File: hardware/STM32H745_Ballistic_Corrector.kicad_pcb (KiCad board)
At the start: 4 copper layers, 80 x 60 mm, 4 parts

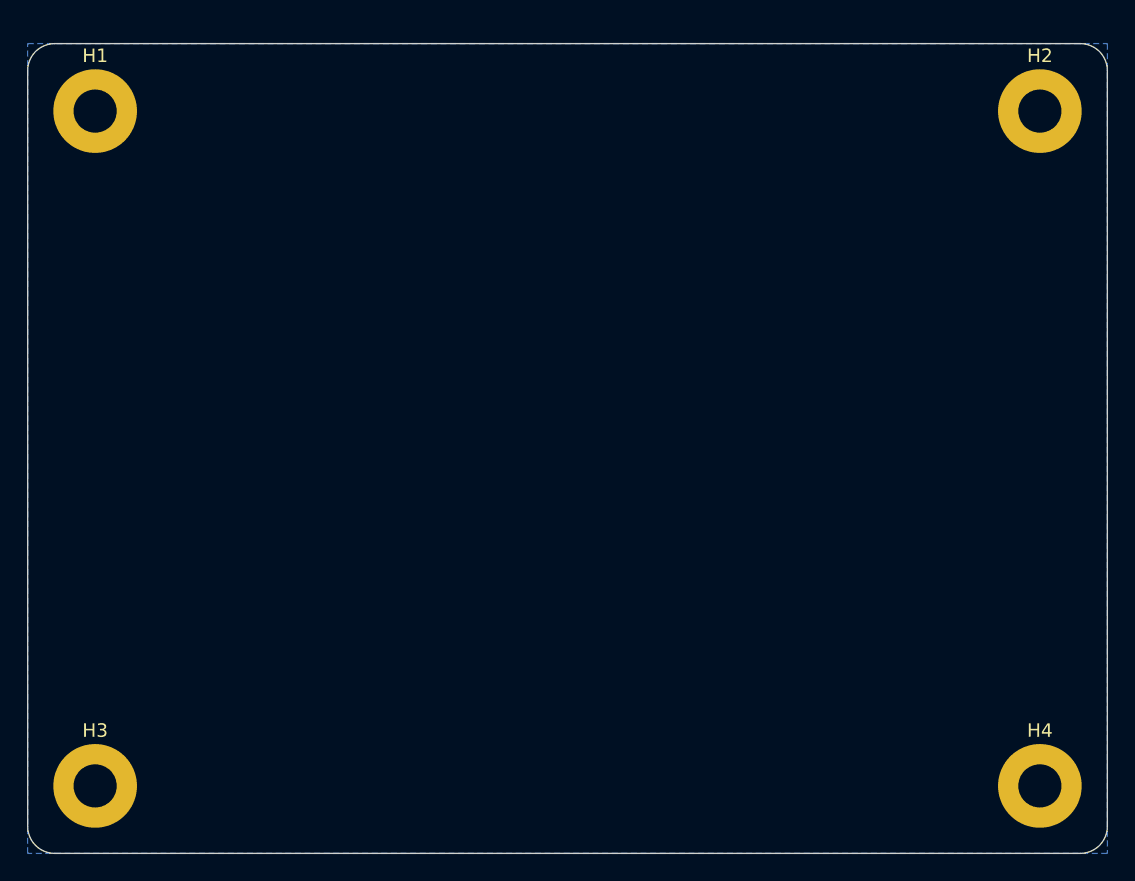
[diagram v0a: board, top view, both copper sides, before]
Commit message: PCB placement pass: 48 component footprints placed per HLD floorplan
Placement generator (tools/gen_pcb_placement.py):
- Reproducible: emits footprints into a marked block of the .kicad_pcb;
  re-running regenerates the block idempotently (deterministic UUIDs)
- Package generators: LQFP-144, QFN-24/28 (+EP), SOIC-8 (150/208 mil),
  MSOP-8, SOT-23-5, SOT-223, LGA-12 (VL53L0X), LGA-10 (BMP390),
  3225 crystal, chip 0402/0805, SMA diode, 4x4 inductor, pin headers
  (1x3, 2x5 1.27mm SWD, 2x7 2.54mm sensor), USB Mini-B, barrel jack,
  slide switch, test points

Placement per HLD_BOARD_INTEGRATION.md §5.3 floorplan:
- POWER row (top edge): J1 12V in -> D1 Schottky -> U2 buck + L1 ->
  U3 3V3 LDO -> U12 1V8 LDO, bulk caps, 6 rail test points TP1-TP6
- DEBUG zone (left): J5 USB, U8 CP2102N, J2 UART header, J3 SWD 2x5,
  SW1 BOOT0, NRST RC (R1/C1), BOOT0 pull-down R4
- MCU zone (center): U1 LQFP-144 at (90,78), Y1 8MHz + 12pF load caps
  in crystal corner, 8x 100nF decoupling ring + 10uF bulk, I2C pull-ups
- MEMORY zone (right): U6 W25Q128JV 25mm from MCU QSPI bank, U7 EEPROM
- SENSOR row (bottom): U5 VL53L0X at board edge (clear aperture),
  U4 ICM-20689 at mount-hole center of mass, U10 MCP9808, U11 BMP390,
  J4 14-pin sensor connector with HLD §5.4 fixed pinout nets

Net binding: power rails, QSPI (U6 full pinout), I2C, SPI, UART, USB
pads pre-assigned to existing PCB nets for ratsnest-guided routing;
provisional until schematic netlist import

Verification: automated courtyard collision + board containment check -
2 initial overlaps (J4/H4, J2/J5) fixed by position adjustment, final
result 52 footprints, 0 overlaps, s-expression balance clean

Co-Authored-By: Claude Fable 5 <noreply@anthropic.com>
Claude-Session: https://claude.ai/code/session_01WTnjtLhvvQkSSzjNBr8Vvw
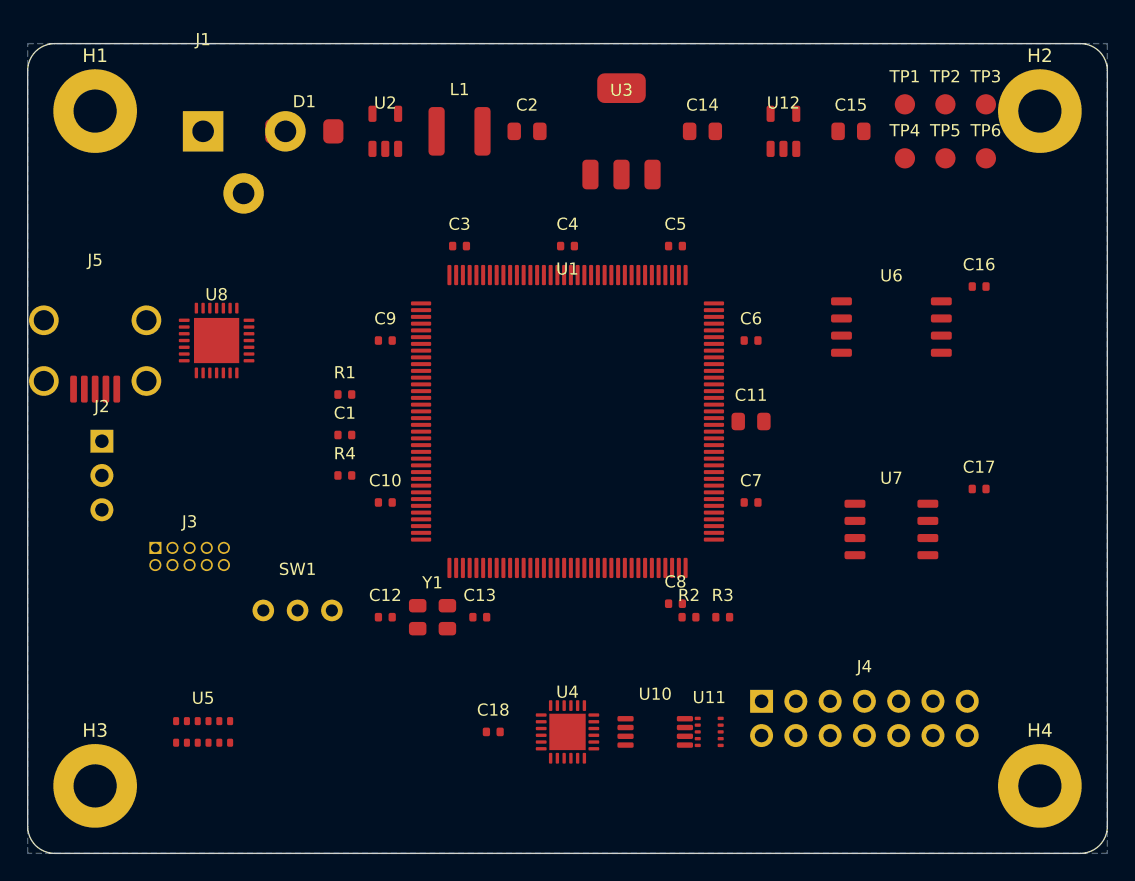
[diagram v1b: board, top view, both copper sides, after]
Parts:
- added C1: 100nF, Capacitor_SMD:C_0402, F.Cu at (73.5, 79.0)
- added C10: 100nF, Capacitor_SMD:C_0402, F.Cu at (76.5, 84.0)
- added C11: 10uF, Capacitor_SMD:C_0805, F.Cu at (103.6, 78.0)
- added C12: 12pF 1%, Capacitor_SMD:C_0402, F.Cu at (76.5, 92.5)
- added C13: 12pF 1%, Capacitor_SMD:C_0402, F.Cu at (83.5, 92.5)
- added C14: 10uF, Capacitor_SMD:C_0805, F.Cu at (100.0, 56.5)
- added C15: 10uF, Capacitor_SMD:C_0805, F.Cu at (111.0, 56.5)
- added C16: 100nF, Capacitor_SMD:C_0402, F.Cu at (120.5, 68.0)
- added C17: 100nF, Capacitor_SMD:C_0402, F.Cu at (120.5, 83.0)
- added C18: 100nF, Capacitor_SMD:C_0402, F.Cu at (84.5, 101.0)
- added C2: 10uF, Capacitor_SMD:C_0805, F.Cu at (87.0, 56.5)
- added C3: 100nF, Capacitor_SMD:C_0402, F.Cu at (82.0, 65.0)
- added C4: 100nF, Capacitor_SMD:C_0402, F.Cu at (90.0, 65.0)
- added C5: 100nF, Capacitor_SMD:C_0402, F.Cu at (98.0, 65.0)
- added C6: 100nF, Capacitor_SMD:C_0402, F.Cu at (103.6, 72.0)
- added C7: 100nF, Capacitor_SMD:C_0402, F.Cu at (103.6, 84.0)
- added C8: 100nF, Capacitor_SMD:C_0402, F.Cu at (98.0, 91.5)
- added C9: 100nF, Capacitor_SMD:C_0402, F.Cu at (76.5, 72.0)
- added D1: 1N5819 SMA, Diode_SMD:D_SMA, F.Cu at (70.5, 56.5)
- added J1: 12V_IN, Connector_BarrelJack:BarrelJack_5.5x2.1mm, F.Cu at (63.0, 56.5)
- added J2: UART_DBG, Connector_PinHeader_2.54mm:PinHeader_1x03, F.Cu at (55.5, 82.0)
- added J3: SWD, Connector_PinHeader_1.27mm:PinHeader_2x05, F.Cu at (62.0, 88.0)
- added J4: SENSOR_14P, Connector_PinHeader_2.54mm:PinHeader_2x07, F.Cu at (112.0, 100.0)
- added J5: USB_MINI_B, Connector_USB:USB_Mini-B, F.Cu at (55.0, 72.0)
- added L1: 4.7uH, Inductor_SMD:L_4x4mm, F.Cu at (82.0, 56.5)
- added R1: 10k, Resistor_SMD:R_0402, F.Cu at (73.5, 76.0)
- added R2: 10k, Resistor_SMD:R_0402, F.Cu at (99.0, 92.5)
- added R3: 10k, Resistor_SMD:R_0402, F.Cu at (101.5, 92.5)
- added R4: 10k, Resistor_SMD:R_0402, F.Cu at (73.5, 82.0)
- added SW1: BOOT0, Button_Switch_THT:SW_Slide, F.Cu at (70.0, 92.0)
- added TP1: VCC_12V, TestPoint:TestPoint_Pad_1.5mm, F.Cu at (115.0, 54.5)
- added TP2: VCC_5V, TestPoint:TestPoint_Pad_1.5mm, F.Cu at (118.0, 54.5)
- added TP3: VCC_3V3, TestPoint:TestPoint_Pad_1.5mm, F.Cu at (121.0, 54.5)
- added TP4: VCC_1V8, TestPoint:TestPoint_Pad_1.5mm, F.Cu at (115.0, 58.5)
- added TP5: GND, TestPoint:TestPoint_Pad_1.5mm, F.Cu at (118.0, 58.5)
- added TP6: GND, TestPoint:TestPoint_Pad_1.5mm, F.Cu at (121.0, 58.5)
- added U1: STM32H745ZIT6, Package_QFP:LQFP-144_20x20mm_P0.5mm, F.Cu at (90.0, 78.0)
- added U10: MCP9808, Package_SO:MSOP-8_3x3mm_P0.65mm, F.Cu at (96.5, 101.0)
- added U11: BMP390, Sensor_Pressure:Bosch_LGA-10, F.Cu at (100.5, 101.0)
- added U12: LDO_1V8_200mA, Package_TO_SOT_SMD:SOT-23-5, F.Cu at (106.0, 56.5)
- added U2: TPS62133A, Package_TO_SOT_SMD:SOT-23-5, F.Cu at (76.5, 56.5)
- added U3: LDO_3V3_500mA, Package_TO_SOT_SMD:SOT-223, F.Cu at (94.0, 56.5)
- added U4: ICM-20689, Package_DFN_QFN:QFN-24_4x4mm_P0.5mm, F.Cu at (90.0, 101.0)
- added U5: VL53L0X, Sensor_Distance:ST_VL53L0X, F.Cu at (63.0, 101.0)
- added U6: W25Q128JV, Package_SO:SOIC-8_5.23x5.23mm_P1.27mm, F.Cu at (114.0, 71.0)
- added U7: AT24C256C, Package_SO:SOIC-8_3.9x4.9mm_P1.27mm, F.Cu at (114.0, 86.0)
- added U8: CP2102N, Package_DFN_QFN:QFN-28_5x5mm_P0.5mm, F.Cu at (64.0, 72.0)
- added Y1: 8MHz, Crystal:Crystal_SMD_3225-4Pin, F.Cu at (80.0, 92.5)

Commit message: PCB: LQFP144 power fan-out + full QSPI routing with geometric self-audit
Routing generator (tools/gen_pcb_routing.py) emits 95 segments + 62 vias:

QSPI U1 <-> U6 (all 6 nets connected, 0.28mm = 50R on this stackup):
- CLK: F.Cu south bus -> east riser -> flash pin 6
- CS:  F.Cu north bus above MCU -> flash pin 1
- D0-D3: F.Cu escape stubs -> B.Cu corridors (over continuous pours) ->
  F.Cu entry stubs; staggered escape vias clear the 0.5mm-pitch stub rows
- U1 pin->net map added to placement generator (QSPI on PB2/PB6/PD11-13/
  PE2, SPI/I2C/UART/USB/NRST/BOOT0, 20 VDD/VSS pins; verify vs datasheet
  at netlist import)

Power fan-out:
- 20 LQFP144 VDD/VSS stub+via pairs to In1 GND / In2 3V3 planes; vias
  tucked inside the package body because QSPI buses own the N/S/E escape
  corridors; staggered diagonals keep 0.5mm-pitch neighbours clear
- Via drops for all decoupling caps (C3-C11, C16-C18), I2C pull-ups,
  U6/U7 supply pins, test-point plane ties

Blind-zone audit (built into generator, aborts on violation):
- segment/segment crossings per layer, segment/via, via/via,
  segment/pad and via/pad clearances against all 52 footprints
- First run: 74 findings -> 6 real conflicts fixed (C7 moved out of the
  D0 corridor, D0/D3 staggered escapes, D1 riser moved west, C6/C11/U7
  via drops relocated, U6 GND via clear of D3 corridor); remainder were
  parser false-positives (pad net attribute), parser fixed
- Final: 0 violations, courtyard check still PASS

QSPI lengths (mm): CLK 54.1, CS 29.5, D0 31.6, D1 25.6, D2 48.5, D3 31.6
-> data skew 22.9mm (~0.15ns); meander tuning pass to +/-0.5mm remains
(free corridors reserved south of U6)

Co-Authored-By: Claude Fable 5 <noreply@anthropic.com>
Claude-Session: https://claude.ai/code/session_01WTnjtLhvvQkSSzjNBr8Vvw
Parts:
- moved C7 2.60 mm to (103.6, 86.6)
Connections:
- U1 pad 1: (no net) -> QSPI_D2
- U1 pad 103: (no net) -> USB_DM
- U1 pad 104: (no net) -> USB_DP
- U1 pad 107: (no net) -> GND
- U1 pad 108: (no net) -> VCC_3V3
- U1 pad 120: (no net) -> GND
- U1 pad 121: (no net) -> VCC_3V3
- U1 pad 130: (no net) -> GND
- U1 pad 131: (no net) -> VCC_3V3
- U1 pad 136: (no net) -> QSPI_CS
- U1 pad 138: (no net) -> BOOT0
- U1 pad 139: (no net) -> I2C1_SCL
- U1 pad 140: (no net) -> I2C1_SDA
- U1 pad 143: (no net) -> GND
- U1 pad 144: (no net) -> VCC_3V3
- U1 pad 16: (no net) -> GND
- U1 pad 17: (no net) -> VCC_3V3
- U1 pad 25: (no net) -> NRST
- U1 pad 36: (no net) -> UART2_TX
- U1 pad 37: (no net) -> UART2_RX
- U1 pad 38: (no net) -> GND
- U1 pad 39: (no net) -> VCC_3V3
- U1 pad 41: (no net) -> SPI1_CLK
- U1 pad 42: (no net) -> SPI1_MISO
- U1 pad 43: (no net) -> SPI1_MOSI
- U1 pad 46: (no net) -> SPI1_CS_IMU
- U1 pad 48: (no net) -> QSPI_CLK
- U1 pad 51: (no net) -> GND
- U1 pad 52: (no net) -> VCC_3V3
- U1 pad 61: (no net) -> GND
- U1 pad 62: (no net) -> VCC_3V3
- U1 pad 72: (no net) -> VCC_3V3
- U1 pad 80: (no net) -> QSPI_D0
- U1 pad 81: (no net) -> QSPI_D1
- U1 pad 82: (no net) -> QSPI_D3
- U1 pad 83: (no net) -> GND
- U1 pad 84: (no net) -> VCC_3V3
- U1 pad 94: (no net) -> GND
- U1 pad 95: (no net) -> VCC_3V3
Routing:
- net QSPI_CLK: track 0.00 -> 54.1 mm
- net QSPI_D2: track 0.00 -> 48.5 mm, vias 0 -> 2
- net VCC_3V3: track 0.00 -> 46.6 mm, vias 0 -> 27
- net GND: track 0.00 -> 38.4 mm, vias 0 -> 26
- net QSPI_D3: track 0.00 -> 31.6 mm, vias 0 -> 2
- net QSPI_D0: track 0.00 -> 31.6 mm, vias 0 -> 2
- net QSPI_CS: track 0.00 -> 29.5 mm
- net QSPI_D1: track 0.00 -> 25.6 mm, vias 0 -> 2
- net VCC_5V: track 0.00 -> 1.20 mm, vias 0 -> 1

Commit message: PCB: QSPI length tuning to 0.01mm skew + SPI/I2C/UART signal routing
QSPI meanders (all on B.Cu, audit-verified):
- D0 +16.97mm north-pocket detour (x112.5..115.8, dip to y77.115)
- D1 +22.90mm west excursion (x90.05, band y71.0..74.3 between power vias)
- D3 +16.96mm south dip (x104.8..109.4 to y82.28)
- Result: D0-D3 all 48.54mm, data skew 0.01mm (budget +/-0.5mm)

Signal routing (HLD step 6):
- SPI1 -> U4 pins 22/23/24 via a via row north of the I2C trunks;
  MISO -> J4.6 with an F.Cu hop across the I2C U7 risers; CS -> J4.8
  through the x=113.2 inter-column corridor
- I2C1 SCL/SDA trees: west descents, south trunks y96.1/96.7, drops to
  U5/U10/J4.3/J4.4/R2/R3/U7; the two topologically-required net
  crossings resolved with planned F.Cu hop via pairs
- UART2 TX/RX -> J2 on west F.Cu
- Audit iterations: 17 -> 6 -> 0 violations; 183 segments, 85 vias,
  courtyard check PASS
- Deferred to KiCad interactive (documented in HLD 5.5 + state journal):
  USB 90R pair (needs coupled routing), SPI CLK/MOSI -> J4 pins 5/7

Co-Authored-By: Claude Fable 5 <noreply@anthropic.com>
Claude-Session: https://claude.ai/code/session_01WTnjtLhvvQkSSzjNBr8Vvw
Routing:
- net I2C1_SDA: track 0.00 -> 174.0 mm, vias 0 -> 6
- net I2C1_SCL: track 0.00 -> 125.3 mm, vias 0 -> 8
- net SPI1_MISO: track 0.00 -> 57.7 mm, vias 0 -> 3
- net SPI1_CS_IMU: track 0.00 -> 51.7 mm, vias 0 -> 2
- net UART2_RX: track 0.00 -> 34.9 mm
- net UART2_TX: track 0.00 -> 30.9 mm
- net QSPI_D1: track 25.6 -> 48.5 mm
- net QSPI_D0: track 31.6 -> 48.5 mm
- net QSPI_D3: track 31.6 -> 48.5 mm
- net SPI1_CLK: track 0.00 -> 16.9 mm, vias 0 -> 2
- net SPI1_MOSI: track 0.00 -> 14.2 mm, vias 0 -> 2
